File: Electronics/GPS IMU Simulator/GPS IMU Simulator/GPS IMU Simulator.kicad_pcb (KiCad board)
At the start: 2 copper layers, 15 parts, among them J1 BUTTON 1, J11 Conn_01x02, J2 TERM, J3 GPS SIM, J4 CAN BUS, J9 JOYSTICK 1, U1 TEENSY 4.0, U2 TJA1462ATK-0Z, U3 PESD2CANFD24V-TR

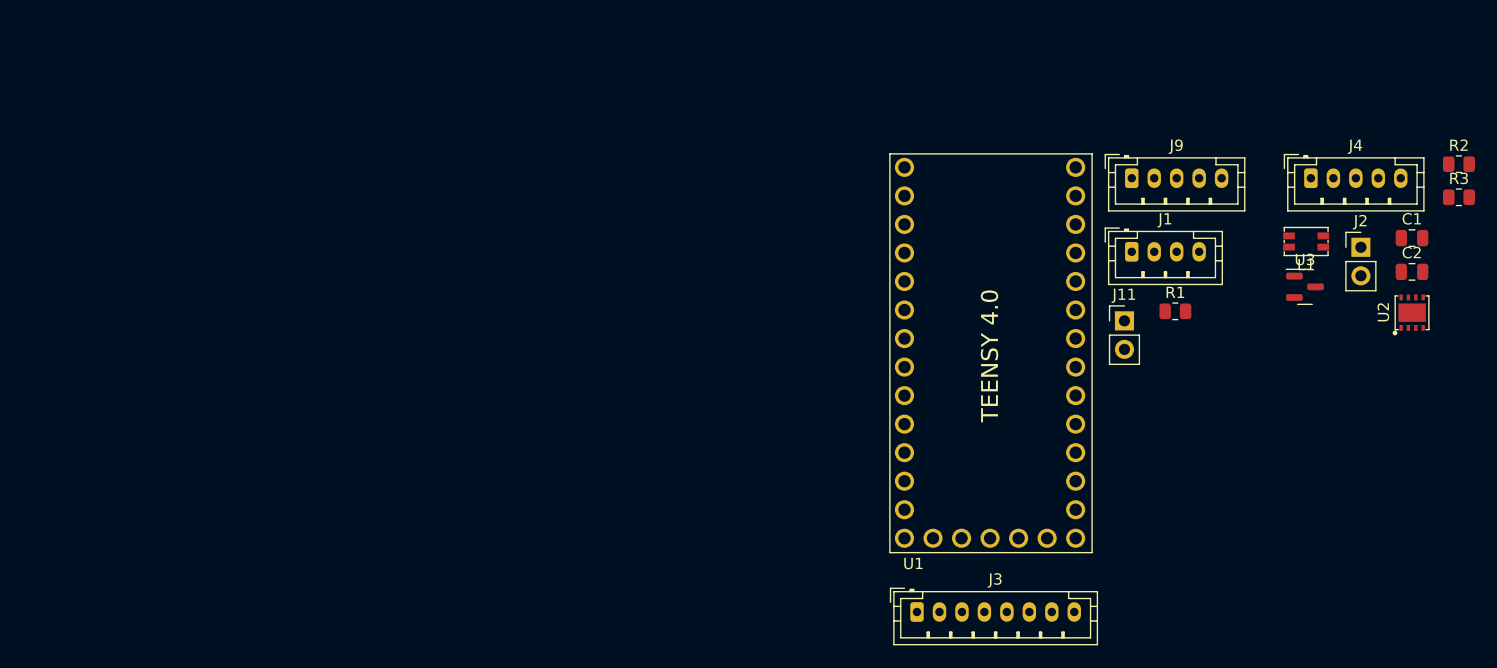
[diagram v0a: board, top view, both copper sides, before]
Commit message: Completed first attempt at GPS/IMU simulator.
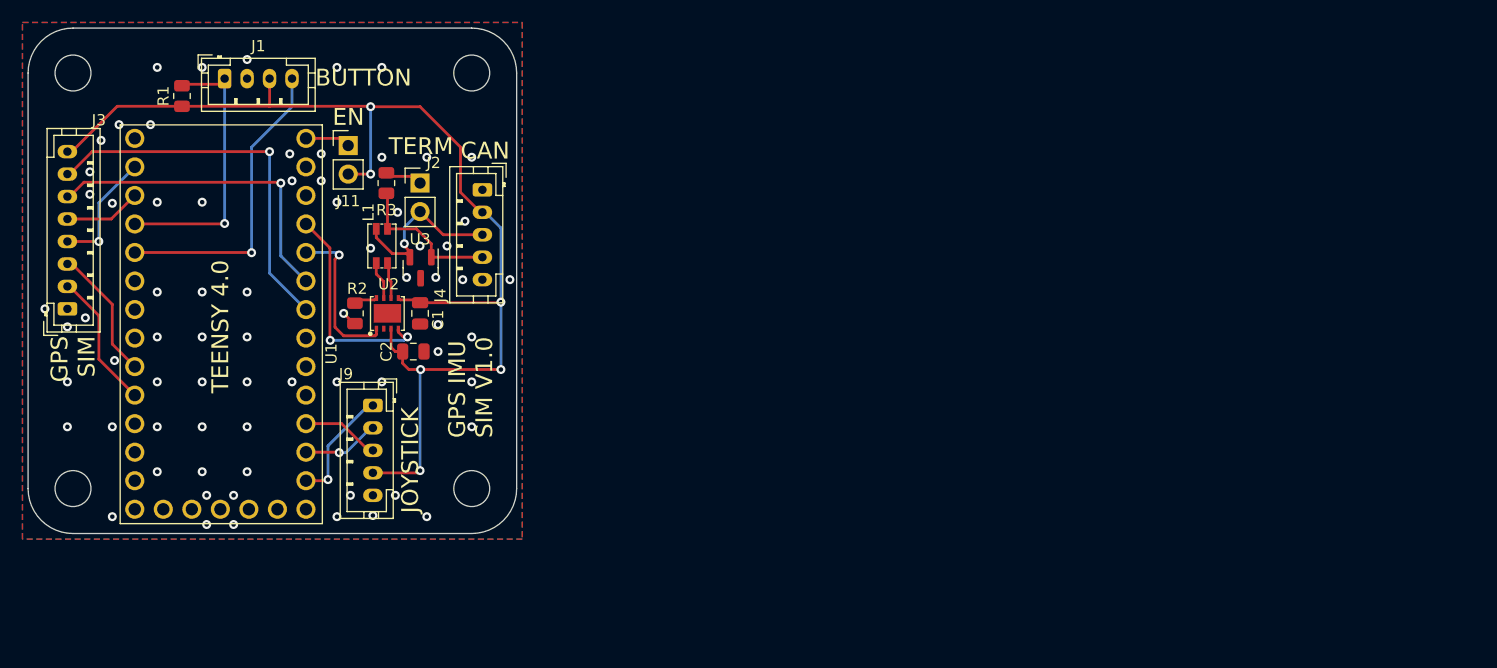
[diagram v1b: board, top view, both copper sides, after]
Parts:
- moved R2 99.2 mm to (171.6, 79.4), turned to 90 degrees
- moved R3 95.5 mm to (174.4, 67.8), turned to 90 degrees
- moved U2 91.2 mm to (173.5, 80.8)
- moved R1 90.5 mm to (156.2, 60.0), turned to 90 degrees
- moved C2 89.2 mm to (176.8, 82.8)
- moved C1 88.6 mm to (177.4, 79.4), turned to -90 degrees
- moved J2 84.0 mm to (177.4, 67.8)
- moved L1 82.3 mm to (174.0, 73.4), turned to 90 degrees
- moved J1 82.2 mm to (160.0, 58.5)
- moved J3 80.3 mm to (146.0, 79.0), turned to 90 degrees
- moved U3 78.8 mm to (177.4, 75.3), turned to -90 degrees
- moved J4 73.8 mm to (182.9, 68.4), turned to -90 degrees
- moved J11 70.9 mm to (171.0, 64.5)
- moved J9 70.5 mm to (173.2, 87.6), turned to -90 degrees
- moved U1 68.6 mm to (152.0, 63.8)
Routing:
- net +5V: track 0.00 -> 105.7 mm, vias 0 -> 6
- net /GNSS/GNSS_TRACTOR_TX: track 0.00 -> 34.2 mm, vias 0 -> 1
- net /GNSS/GNSS_TRACTOR_RX: track 0.00 -> 29.2 mm, vias 0 -> 1
- net /B1_LED_GND: track 0.00 -> 27.4 mm, vias 0 -> 1
- net /B1: track 0.00 -> 25.0 mm, vias 0 -> 1
- net /CAN/CAN_RX: track 0.00 -> 19.6 mm, vias 0 -> 2
- net /CAN/CAN_H: track 0.00 -> 15.8 mm, vias 0 -> 1
- net /CAN/CAN_TX: track 0.00 -> 14.2 mm, vias 0 -> 1
- net /CAN/CAN_L: track 0.00 -> 13.4 mm
- net /GNSS/GNSS_REAR_TX: track 0.00 -> 12.3 mm
- net /GNSS/GNSS_REAR_RX: track 0.00 -> 11.9 mm
- net /GNSS/GNSS_FRONT_RX: track 0.00 -> 10.8 mm, vias 0 -> 1
- net /J1_SW: track 0.00 -> 10.5 mm, vias 0 -> 1
- net /J1_X: track 0.00 -> 6.95 mm
- net /J1_Y: track 0.00 -> 6.89 mm, vias 0 -> 1
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- added copper zone on B.Cu, net GND
- added copper zone on F.Cu, net GND
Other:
- board outline added: 43.5 x 45 mm
- board text added: "(C) ANDY@BRITISHIDEAS.COM"
- board text added: "BUTTON"
- board text added: "CAN"
- board text added: "EN"
- board text added: "GPS IMU SIM V1.0"
- board text added: "GPS SIM"
- board text added: "JOYSTICK"
- board text added: "TERM"

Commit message: Removed JLCPCB part numbers for Teensy and BNO085 connectors. Added JLCPCB part number for 4.7uF capacitor. Generated JLCPCB manufacturing files for all boards.
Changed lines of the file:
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@@
     (fp_line (start 1 0.625) (end -1 0.625)
       (stroke (width 0.1) (type solid)) (layer "F.Fab"))
-    (pad "1" smd roundrect (at -0.9125 0 90) (size 1.025 1.4) (layers "F.Cu" "F.Paste" "F.Mask") (roundrect_rratio 0.243902)
+    (pad "1" smd roundrect (at -0.9125 0 90) (size 1.025 1.4) (layers "F.Cu" "F.Paste" "F.Mask") (roundrect_rratio 0.243902439)
       (net 2 "GND") (pintype "passive"))
-    (pad "2" smd roundrect (at 0.9125 0 90) (size 1.025 1.4) (layers "F.Cu" "F.Paste" "F.Mask") (roundrect_rratio 0.243902)
+    (pad "2" smd roundrect (at 0.9125 0 90) (size 1.025 1.4) (layers "F.Cu" "F.Paste" "F.Mask") (roundrect_rratio 0.243902439)
       (net 21 "Net-(U2-STB)") (pintype "passive"))
     (model "${KICAD6_3DMODEL_DIR}/Resistor_SMD.3dshapes/R_0805_2012Metric.wrl"
@@
     (fp_line (start 9.95 2.8) (end 9.95 -1.7)
       (stroke (width 0.1) (type solid)) (layer "F.Fab"))
-    (pad "1" thru_hole roundrect (at 0 0 270) (size 1.2 1.75) (drill 0.75) (layers "*.Cu" "*.Mask") (roundrect_rratio 0.208333)
+    (pad "1" thru_hole roundrect (at 0 0 270) (size 1.2 1.75) (drill 0.75) (layers "*.Cu" "*.Mask") (roundrect_rratio 0.2083333333)
       (net 15 "/J1_SW") (pinfunction "Pin_1") (pintype "passive"))
     (pad "2" thru_hole oval (at 2 0 270) (size 1.2 1.75) (drill 0.75) (layers "*.Cu" "*.Mask")
@@
     (fp_line (start 1 0.625) (end -1 0.625)
       (stroke (width 0.1) (type solid)) (layer "F.Fab"))
-    (pad "1" smd roundrect (at -0.9125 0 90) (size 1.025 1.4) (layers "F.Cu" "F.Paste" "F.Mask") (roundrect_rratio 0.243902)
+    (pad "1" smd roundrect (at -0.9125 0 90) (size 1.025 1.4) (layers "F.Cu" "F.Paste" "F.Mask") (roundrect_rratio 0.243902439)
       (net 14 "/CAN/CAN_L") (pintype "passive"))
-    (pad "2" smd roundrect (at 0.9125 0 90) (size 1.025 1.4) (layers "F.Cu" "F.Paste" "F.Mask") (roundrect_rratio 0.243902)
+    (pad "2" smd roundrect (at 0.9125 0 90) (size 1.025 1.4) (layers "F.Cu" "F.Paste" "F.Mask") (roundrect_rratio 0.243902439)
       (net 5 "Net-(J2-Pin_1)") (pintype "passive"))
     (model "${KICAD6_3DMODEL_DIR}/Resistor_SMD.3dshapes/R_0805_2012Metric.wrl"
@@
     (fp_line (start 7.95 2.8) (end 7.95 -1.7)
       (stroke (width 0.1) (type solid)) (layer "F.Fab"))
-    (pad "1" thru_hole roundrect (at 0 0) (size 1.2 1.75) (drill 0.75) (layers "*.Cu" "*.Mask") (roundrect_rratio 0.208333)
+    (pad "1" thru_hole roundrect (at 0 0) (size 1.2 1.75) (drill 0.75) (layers "*.Cu" "*.Mask") (roundrect_rratio 0.2083333333)
       (net 3 "/B1") (pinfunction "Pin_1") (pintype "passive"))
     (pad "2" thru_hole oval (at 2 0) (size 1.2 1.75) (drill 0.75) (layers "*.Cu" "*.Mask")
@@
     (fp_line (start 1 0.625) (end -1 0.625)
       (stroke (width 0.1) (type solid)) (layer "F.Fab"))
-    (pad "1" smd roundrect (at -0.9125 0 90) (size 1.025 1.4) (layers "F.Cu" "F.Paste" "F.Mask") (roundrect_rratio 0.243902)
+    (pad "1" smd roundrect (at -0.9125 0 90) (size 1.025 1.4) (layers "F.Cu" "F.Paste" "F.Mask") (roundrect_rratio 0.243902439)
       (net 1 "+5V") (pintype "passive"))
-    (pad "2" smd roundrect (at 0.9125 0 90) (size 1.025 1.4) (layers "F.Cu" "F.Paste" "F.Mask") (roundrect_rratio 0.243902)
+    (pad "2" smd roundrect (at 0.9125 0 90) (size 1.025 1.4) (layers "F.Cu" "F.Paste" "F.Mask") (roundrect_rratio 0.243902439)
       (net 3 "/B1") (pintype "passive"))
     (model "${KICAD6_3DMODEL_DIR}/Resistor_SMD.3dshapes/R_0805_2012Metric.wrl"
@@
     (fp_line (start 15.95 2.8) (end 15.95 -1.7)
       (stroke (width 0.1) (type solid)) (layer "F.Fab"))
-    (pad "1" thru_hole roundrect (at 0 0 90) (size 1.2 1.75) (drill 0.75) (layers "*.Cu" "*.Mask") (roundrect_rratio 0.208333)
+    (pad "1" thru_hole roundrect (at 0 0 90) (size 1.2 1.75) (drill 0.75) (layers "*.Cu" "*.Mask") (roundrect_rratio 0.2083333333)
       (net 2 "GND") (pinfunction "Pin_1") (pintype "passive"))
     (pad "2" thru_hole oval (at 2 0 90) (size 1.2 1.75) (drill 0.75) (layers "*.Cu" "*.Mask")
@@
     (fp_line (start 9.95 2.8) (end 9.95 -1.7)
       (stroke (width 0.1) (type solid)) (layer "F.Fab"))
-    (pad "1" thru_hole roundrect (at 0 0 270) (size 1.2 1.75) (drill 0.75) (layers "*.Cu" "*.Mask") (roundrect_rratio 0.208333)
+    (pad "1" thru_hole roundrect (at 0 0 270) (size 1.2 1.75) (drill 0.75) (layers "*.Cu" "*.Mask") (roundrect_rratio 0.2083333333)
       (net 13 "+12V") (pinfunction "Pin_1") (pintype "passive"))
     (pad "2" thru_hole oval (at 2 0 270) (size 1.2 1.75) (drill 0.75) (layers "*.Cu" "*.Mask")

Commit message: Added fiducials to all boards.
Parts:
- added FID1: Fiducial, Fiducial:Fiducial_0.5mm_Mask1mm, F.Cu at (152.2, 56.2)
- added FID2: Fiducial, Fiducial:Fiducial_0.5mm_Mask1mm, F.Cu at (176.6, 56.2)
- added FID3: Fiducial, Fiducial:Fiducial_0.5mm_Mask1mm, F.Cu at (144.4, 90.6)
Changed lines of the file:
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@@
     (descr "Resistor SMD 0805 (2012 Metric), square (rectangular) end terminal, IPC_7351 nominal, (Body size source: IPC-SM-782 page 72, https://www.pcb-3d.com/wordpress/wp-content/uploads/ipc-sm-782a_amendment_1_and_2.pdf), generated with kicad-footprint-generator")
     (tags "resistor")
+    (property "LCSC" "C17414")
     (property "Sheetfile" "CAN.kicad_sch")
     (property "Sheetname" "CAN")
@@
     (descr "JST PH series connector, B5B-PH-K (http://www.jst-mfg.com/product/pdf/eng/ePH.pdf), generated with kicad-footprint-generator")
     (tags "connector JST PH side entry")
+    (property "LCSC" "C157993")
     (property "Sheetfile" "GPS IMU Simulator.kicad_sch")
     (property "Sheetname" "")
@@
     )
   )
+  (footprint "Fiducial:Fiducial_0.5mm_Mask1mm" (layer "F.Cu")
+    (at 176.6 56.2)
+    (descr "Circular Fiducial, 0.5mm bare copper, 1mm soldermask opening (Level C)")
+    (tags "fiducial")
+    (property "Sheetfile" "GPS IMU Simulator.kicad_sch")
+    (property "Sheetname" "")
+    (property "ki_description" "Fiducial Marker")
+    (property "ki_keywords" "fiducial marker")
+    (attr smd)
+    (fp_text reference "FID2" (at 0 -1.5) (layer "F.SilkS") hide
+        (effects (font (size 1 1) (thickness 0.15)))
+    )
+    (fp_text value "Fiducial" (at 0 1.5) (layer "F.Fab")
+        (effects (font (size 1 1) (thickness 0.15)))
+    )
+    (fp_text user "${REFERENCE}" (at 0 0) (layer "F.Fab")
+        (effects (font (size 0.2 0.2) (thickness 0.04)))
+    )
+    (fp_circle (center 0 0) (end 0.75 0)
+      (stroke (width 0.05) (type solid)) (fill none) (layer "F.CrtYd"))
+    (fp_circle (center 0 0) (end 0.5 0)
+      (stroke (width 0.1) (type solid)) (fill none) (layer "F.Fab"))
+    (pad "" smd circle (at 0 0) (size 0.5 0.5) (layers "F.Cu" "F.Mask")
+      (solder_mask_margin 0.25) (clearance 0.25))
+  )
   (footprint "Resistor_SMD:R_0805_2012Metric" (layer "F.Cu")
     (at 174.4 67.8 90)
     (descr "Resistor SMD 0805 (2012 Metric), square (rectangular) end terminal, IPC_7351 nominal, (Body size source: IPC-SM-782 page 72, https://www.pcb-3d.com/wordpress/wp-content/uploads/ipc-sm-782a_amendment_1_and_2.pdf), generated with kicad-footprint-generator")
     (tags "resistor")
+    (property "LCSC" "C17437")
     (property "Sheetfile" "CAN.kicad_sch")
     (property "Sheetname" "CAN")
@@
     (at 174 73.4 90)
     (descr "CAN and CANFD Common Mode Choke")
+    (property "LCSC" "C95572")
     (property "Sheetfile" "CAN.kicad_sch")
     (property "Sheetname" "CAN")
@@
     (descr "Through hole straight pin header, 1x02, 2.54mm pitch, single row")
     (tags "Through hole pin header THT 1x02 2.54mm single row")
+    (property "LCSC" "C7494857")
     (property "Sheetfile" "CAN.kicad_sch")
     (property "Sheetname" "CAN")
@@
     (descr "JST PH series connector, B4B-PH-K (http://www.jst-mfg.com/product/pdf/eng/ePH.pdf), generated with kicad-footprint-generator")
     (tags "connector JST PH side entry")
+    (property "LCSC" "C131334")
     (property "Sheetfile" "GPS IMU Simulator.kicad_sch")
     (property "Sheetname" "")
@@
     (descr "Capacitor SMD 0805 (2012 Metric), square (rectangular) end terminal, IPC_7351 nominal, (Body size source: IPC-SM-782 page 76, https://www.pcb-3d.com/wordpress/wp-content/uploads/ipc-sm-782a_amendment_1_and_2.pdf, https://docs.google.com/spreadsheets/d/1BsfQQcO9C6DZCsRaXUlFlo91Tg2WpOkGARC1WS5S8t0/edit?usp=sharing), generated with kicad-footprint-generator")
     (tags "capacitor")
+    (property "LCSC" "C1711")
     (property "Sheetfile" "CAN.kicad_sch")
     (property "Sheetname" "CAN")
@@
     (descr "SOT, 3 Pin (https://www.jedec.org/system/files/docs/to-236h.pdf variant AB), generated with kicad-footprint-generator ipc_gullwing_generator.py")
     (tags "SOT TO_SOT_SMD")
+    (property "LCSC" "C552486")
     (property "Sheetfile" "CAN.kicad_sch")
     (property "Sheetname" "CAN")
@@
     )
   )
+  (footprint "Fiducial:Fiducial_0.5mm_Mask1mm" (layer "F.Cu")
+    (at 144.4 90.6)
+    (descr "Circular Fiducial, 0.5mm bare copper, 1mm soldermask opening (Level C)")
+    (tags "fiducial")
+    (property "Sheetfile" "GPS IMU Simulator.kicad_sch")
+    (property "Sheetname" "")
+    (property "ki_description" "Fiducial Marker")
+    (property "ki_keywords" "fiducial marker")
+    (attr smd)
+    (fp_text reference "FID3" (at 0 -1.5) (layer "F.SilkS") hide
+        (effects (font (size 1 1) (thickness 0.15)))
+    )
+    (fp_text value "Fiducial" (at 0 1.5) (layer "F.Fab")
+        (effects (font (size 1 1) (thickness 0.15)))
+    )
+    (fp_text user "${REFERENCE}" (at 0 0) (layer "F.Fab")
+        (effects (font (size 0.2 0.2) (thickness 0.04)))
+    )
+    (fp_circle (center 0 0) (end 0.75 0)
+      (stroke (width 0.05) (type solid)) (fill none) (layer "F.CrtYd"))
+    (fp_circle (center 0 0) (end 0.5 0)
+      (stroke (width 0.1) (type solid)) (fill none) (layer "F.Fab"))
+    (pad "" smd circle (at 0 0) (size 0.5 0.5) (layers "F.Cu" "F.Mask")
+      (solder_mask_margin 0.25) (clearance 0.25))
+  )
+  (footprint "Fiducial:Fiducial_0.5mm_Mask1mm" (layer "F.Cu")
+    (at 152.2 56.2)
+    (descr "Circular Fiducial, 0.5mm bare copper, 1mm soldermask opening (Level C)")
+    (tags "fiducial")
+    (property "Sheetfile" "GPS IMU Simulator.kicad_sch")
+    (property "Sheetname" "")
+    (property "ki_description" "Fiducial Marker")
+    (property "ki_keywords" "fiducial marker")
+    (attr smd)
+    (fp_text reference "FID1" (at 0 -1.5) (layer "F.SilkS") hide
+        (effects (font (size 1 1) (thickness 0.15)))
+    )
+    (fp_text value "Fiducial" (at 0 1.5) (layer "F.Fab")
+        (effects (font (size 1 1) (thickness 0.15)))
+    )
+    (fp_text user "${REFERENCE}" (at 0 0) (layer "F.Fab")
+        (effects (font (size 0.2 0.2) (thickness 0.04)))
+    )
+    (fp_circle (center 0 0) (end 0.75 0)
+      (stroke (width 0.05) (type solid)) (fill none) (layer "F.CrtYd"))
+    (fp_circle (center 0 0) (end 0.5 0)
+      (stroke (width 0.1) (type solid)) (fill none) (layer "F.Fab"))
+    (pad "" smd circle (at 0 0) (size 0.5 0.5) (layers "F.Cu" "F.Mask")
+      (solder_mask_margin 0.25) (clearance 0.25))
+  )
   (footprint "Resistor_SMD:R_0805_2012Metric" (layer "F.Cu")
     (at 156.2 60.05 90)
     (descr "Resistor SMD 0805 (2012 Metric), square (rectangular) end terminal, IPC_7351 nominal, (Body size source: IPC-SM-782 page 72, https://www.pcb-3d.com/wordpress/wp-content/uploads/ipc-sm-782a_amendment_1_and_2.pdf), generated with kicad-footprint-generator")
     (tags "resistor")
+    (property "LCSC" "C17414")
     (property "Sheetfile" "GPS IMU Simulator.kicad_sch")
     (property "Sheetname" "")
@@
     (descr "JST PH series connector, B8B-PH-K (http://www.jst-mfg.com/product/pdf/eng/ePH.pdf), generated with kicad-footprint-generator")
     (tags "connector JST PH side entry")
+    (property "LCSC" "C157974")
     (property "Sheetfile" "GNSS.kicad_sch")
     (property "Sheetname" "GNSS")
@@
   (footprint "Britishideas:Teensy_4.0" (layer "F.Cu")
     (at 152 63.82)
+    (property "LCSC" "")
     (property "Sheetfile" "GPS IMU Simulator.kicad_sch")
     (property "Sheetname" "")
@@
     (descr "JST PH series connector, B5B-PH-K (http://www.jst-mfg.com/product/pdf/eng/ePH.pdf), generated with kicad-footprint-generator")
     (tags "connector JST PH side entry")
+    (property "LCSC" "C157993")
     (property "Sheetfile" "CAN.kicad_sch")
     (property "Sheetname" "CAN")
@@
     (descr "Capacitor SMD 0805 (2012 Metric), square (rectangular) end terminal, IPC_7351 nominal, (Body size source: IPC-SM-782 page 76, https://www.pcb-3d.com/wordpress/wp-content/uploads/ipc-sm-782a_amendment_1_and_2.pdf, https://docs.google.com/spreadsheets/d/1BsfQQcO9C6DZCsRaXUlFlo91Tg2WpOkGARC1WS5S8t0/edit?usp=sharing), generated with kicad-footprint-generator")
     (tags "capacitor")
+    (property "LCSC" "C1711")
     (property "Sheetfile" "CAN.kicad_sch")
     (property "Sheetname" "CAN")
@@
     (at 173.5153 80.76375)
     (descr "aka SOT782-1")
+    (property "LCSC" "C3229259")
     (property "Sheetfile" "CAN.kicad_sch")
     (property "Sheetname" "CAN")
@@
     (descr "Through hole straight pin header, 1x02, 2.54mm pitch, single row")
     (tags "Through hole pin header THT 1x02 2.54mm single row")
+    (property "LCSC" "C7494857")
     (property "Sheetfile" "GPS IMU Simulator.kicad_sch")
     (property "Sheetname" "")
